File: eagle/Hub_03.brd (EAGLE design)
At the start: 24.3 x 59 mm, 16 parts, among them IC1 ATTINY85-20PU, Q1 IRFZ44NPBFS

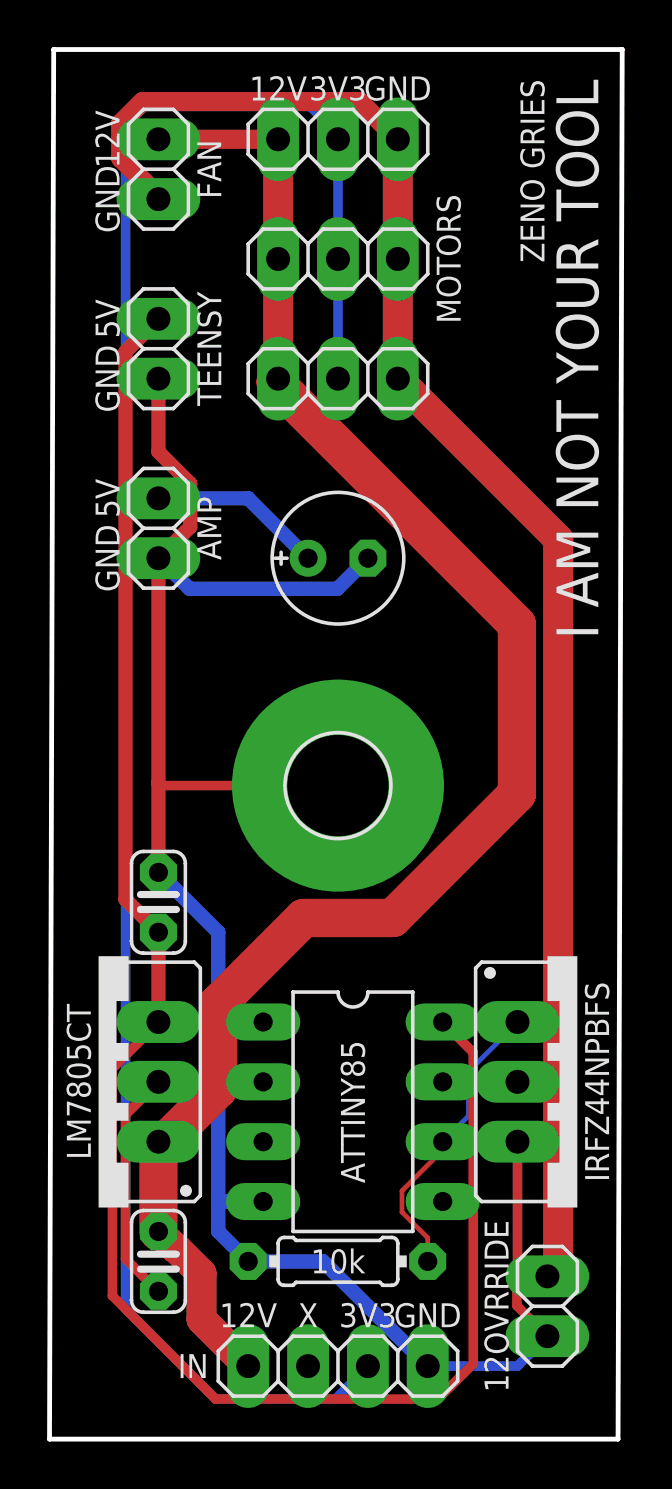
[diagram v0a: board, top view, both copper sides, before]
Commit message: added new hub
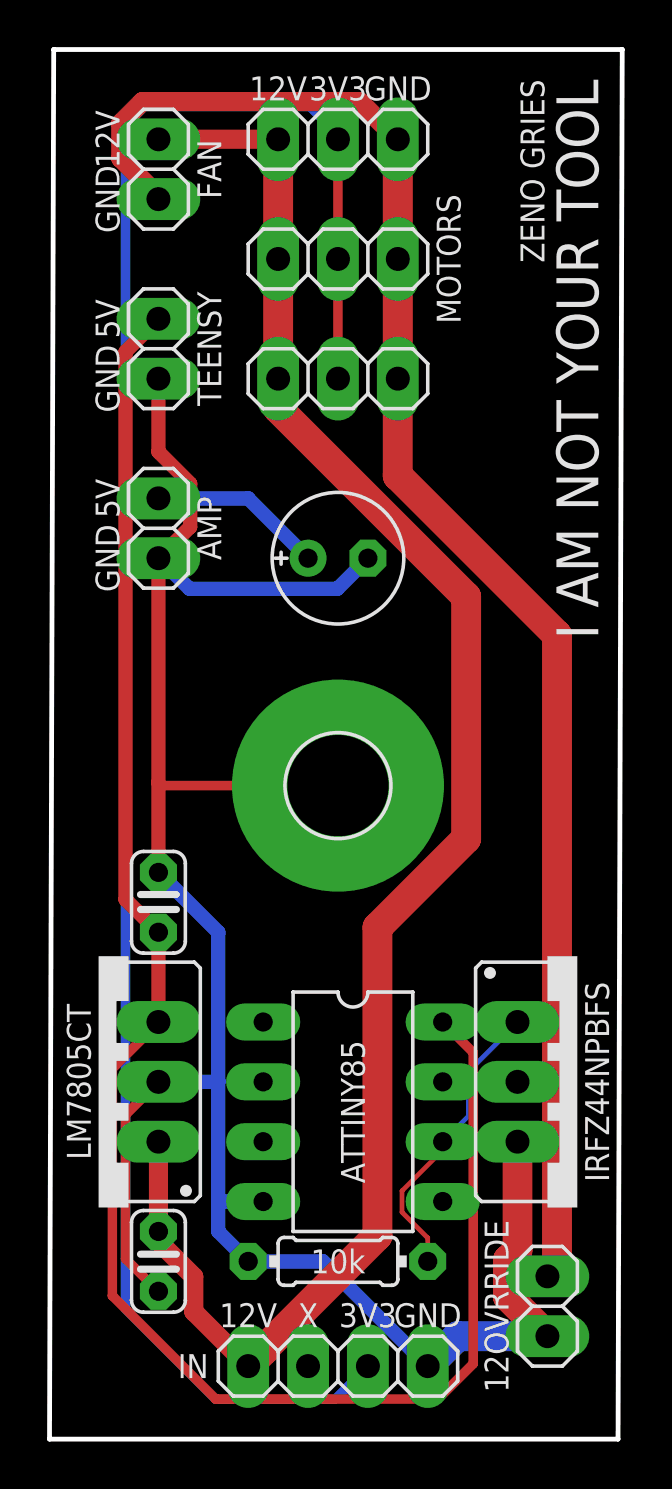
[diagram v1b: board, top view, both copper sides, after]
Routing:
- net MOTOR: track 122.7 -> 69.6 mm
- net +12V: track 89.6 -> 75.4 mm
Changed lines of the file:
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@@
 <wire x1="0" y1="29.21" x2="0.0198625" y2="29.21" width="0.6096" layer="1"/>
 <wire x1="1.3462" y1="32.3794625" x2="0" y2="33.7256625" width="0.6096" layer="1"/>
-<wire x1="11.43" y1="-5.08" x2="15.24" y2="-5.08" width="0.4064" layer="16"/>
-<wire x1="15.24" y1="-5.08" x2="16.51" y2="-3.81" width="0.4064" layer="16"/>
-<wire x1="15.2146" y1="-0.733425" x2="15.2146" y2="-2.517775" width="0.4064" layer="1"/>
-<wire x1="16.51" y1="-3.81" x2="16.506825" y2="-3.81" width="0.4064" layer="1"/>
-<wire x1="16.506825" y1="-3.81" x2="15.2146" y2="-2.517775" width="0.4064" layer="1"/>
-<wire x1="15.24" y1="4.445" x2="15.24" y2="-0.708025" width="0.4064" layer="1"/>
-<wire x1="15.24" y1="-0.708025" x2="15.2146" y2="-0.733425" width="0.4064" layer="1"/>
 <wire x1="7.62" y1="19.558" x2="0.127" y2="19.558" width="0.4064" layer="1"/>
 <wire x1="0.127" y1="19.558" x2="0" y2="19.685" width="0.4064" layer="1"/>
@@
 <wire x1="-0.01369375" y1="-1.905" x2="-1.397" y2="-0.52169375" width="0.4064" layer="1"/>
 <wire x1="-1.397" y1="-0.52169375" x2="-1.397" y2="5.5824625" width="0.4064" layer="1"/>
+<wire x1="11.43" y1="-5.08" x2="12.7" y2="-3.81" width="1.27" layer="16"/>
+<wire x1="12.7" y1="-3.81" x2="16.51" y2="-3.81" width="1.27" layer="16"/>
+<wire x1="14.8336" y1="-0.57560625" x2="15.24" y2="-0.16920625" width="1.27" layer="1"/>
+<wire x1="15.24" y1="-0.16920625" x2="15.24" y2="4.445" width="1.27" layer="1"/>
+<wire x1="16.51" y1="-3.81" x2="14.8336" y2="-2.1336" width="1.27" layer="1"/>
+<wire x1="14.8336" y1="-2.1336" x2="14.8336" y2="-0.57560625" width="1.27" layer="1"/>
 </signal>
 <signal name="+12V" class="2">
@@
 <contactref element="IN" pad="4"/>
 <contactref element="C5" pad="1"/>
-<wire x1="0" y1="4.445" x2="0.19" y2="4.445" width="1.27" layer="16"/>
-<wire x1="5.08" y1="36.83" x2="5.08" y2="41.91" width="1.27" layer="16"/>
-<wire x1="5.08" y1="41.91" x2="5.08" y2="46.99" width="1.27" layer="16"/>
-<wire x1="0" y1="4.445" x2="0.19" y2="4.445" width="1.27" layer="1"/>
+<wire x1="0" y1="46.99" x2="5.08" y2="46.99" width="0.8128" layer="1"/>
+<wire x1="3.81" y1="-5.08" x2="4.5212" y2="-4.3688" width="1.27" layer="1"/>
+<wire x1="4.5212" y1="-4.3688" x2="4.5212" y2="-4.32248125" width="1.27" layer="1"/>
+<wire x1="4.5212" y1="-4.32248125" x2="9.2964" y2="0.45271875" width="1.27" layer="1"/>
+<wire x1="9.2964" y1="0.45271875" x2="9.2964" y2="13.54135625" width="1.27" layer="1"/>
+<wire x1="9.2964" y1="13.54135625" x2="13.0598" y2="17.30475625" width="1.27" layer="1"/>
+<wire x1="13.0598" y1="27.5802" x2="5.08" y2="35.56" width="1.27" layer="1"/>
+<wire x1="5.08" y1="35.56" x2="5.08" y2="36.83" width="1.27" layer="1"/>
+<wire x1="13.0598" y1="17.30475625" x2="13.0598" y2="27.5802" width="1.27" layer="1"/>
 <wire x1="5.08" y1="36.83" x2="5.08" y2="41.91" width="1.27" layer="1"/>
 <wire x1="5.08" y1="41.91" x2="5.08" y2="46.99" width="1.27" layer="1"/>
-<wire x1="1.8288" y1="-1.14748125" x2="0.75751875" y2="-0.0762" width="1.27" layer="16"/>
-<wire x1="3.81" y1="-5.08" x2="1.8288" y2="-3.0988" width="1.27" layer="16"/>
-<wire x1="0.75751875" y1="-0.0762" x2="0.7112" y2="-0.0762" width="1.27" layer="16"/>
-<wire x1="0.7112" y1="-0.0762" x2="0" y2="0.635" width="1.27" layer="16"/>
-<wire x1="1.8288" y1="-3.0988" x2="1.8288" y2="-1.14748125" width="1.27" layer="16"/>
-<wire x1="1.8288" y1="-1.14748125" x2="0.75751875" y2="-0.0762" width="1.27" layer="1"/>
-<wire x1="3.81" y1="-5.08" x2="1.8288" y2="-3.0988" width="1.27" layer="1"/>
-<wire x1="0.75751875" y1="-0.0762" x2="0.7112" y2="-0.0762" width="1.27" layer="1"/>
-<wire x1="0.7112" y1="-0.0762" x2="0" y2="0.635" width="1.27" layer="1"/>
-<wire x1="1.8288" y1="-3.0988" x2="1.8288" y2="-1.14748125" width="1.27" layer="1"/>
-<wire x1="0" y1="46.99" x2="5.08" y2="46.99" width="0.8128" layer="1"/>
-<wire x1="0" y1="0.635" x2="0" y2="4.445" width="1.6256" layer="1"/>
-<wire x1="0" y1="4.445" x2="0.2977625" y2="4.445" width="1.6256" layer="1"/>
-<wire x1="2.54" y1="6.6872375" x2="0.2977625" y2="4.445" width="1.6256" layer="1"/>
-<wire x1="2.54" y1="6.6872375" x2="2.54" y2="10.31408125" width="1.6256" layer="1"/>
-<wire x1="2.54" y1="10.31408125" x2="6.16631875" y2="13.9404" width="1.6256" layer="1"/>
-<wire x1="6.16631875" y1="13.9404" x2="9.9468875" y2="13.9404" width="1.6256" layer="1"/>
-<wire x1="9.9468875" y1="13.9404" x2="15.2146" y2="19.2081125" width="1.6256" layer="1"/>
-<wire x1="5.08" y1="36.83" x2="4.9784" y2="36.7284" width="1.6256" layer="1"/>
-<wire x1="4.9784" y1="36.7284" x2="4.9784" y2="36.6338375" width="1.6256" layer="1"/>
-<wire x1="15.2146" y1="26.3976375" x2="4.9784" y2="36.6338375" width="1.6256" layer="1"/>
-<wire x1="15.2146" y1="19.2081125" x2="15.2146" y2="26.3976375" width="1.6256" layer="1"/>
+<wire x1="3.81" y1="-5.08" x2="1.4986" y2="-2.7686" width="0.8128" layer="1"/>
+<wire x1="0" y1="0.21434375" x2="0" y2="0.635" width="0.8128" layer="1"/>
+<wire x1="1.4986" y1="-2.7686" x2="1.4986" y2="-1.28425625" width="0.8128" layer="1"/>
+<wire x1="1.4986" y1="-1.28425625" x2="0" y2="0.21434375" width="0.8128" layer="1"/>
+<wire x1="0" y1="0.635" x2="0" y2="4.445" width="0.8128" layer="1"/>
 </signal>
 <signal name="+5V" class="3">
@@
 <wire x1="7.62" y1="46.99" x2="7.62" y2="47.20434375" width="0.4064" layer="16"/>
 <wire x1="7.62" y1="47.20434375" x2="6.43734375" y2="48.387" width="0.4064" layer="16"/>
-<wire x1="7.62" y1="46.99" x2="7.62" y2="41.91" width="0.4064" layer="16"/>
-<wire x1="7.62" y1="41.91" x2="7.62" y2="36.83" width="0.4064" layer="16"/>
 <wire x1="8.89" y1="-5.1054" x2="8.89" y2="-5.08" width="0.4064" layer="16"/>
 <wire x1="8.89" y1="-5.1054" x2="7.5184" y2="-6.477" width="0.4064" layer="16"/>
 <wire x1="2.42650625" y1="-6.477" x2="7.5184" y2="-6.477" width="0.4064" layer="16"/>
+<wire x1="7.62" y1="46.99" x2="7.62" y2="41.91" width="0.4064" layer="1"/>
+<wire x1="7.62" y1="41.91" x2="7.62" y2="36.83" width="0.4064" layer="1"/>
 </signal>
 <signal name="MOTOR" class="1">
@@
 <contactref element="FAN" pad="1"/>
 <contactref element="MOTORSWITCH" pad="2"/>
-<wire x1="16.9672" y1="30.0228" x2="16.9672" y2="6.985" width="1.27" layer="16"/>
-<wire x1="16.9672" y1="6.985" x2="16.9672" y2="-0.8128" width="1.27" layer="16"/>
-<wire x1="16.51" y1="-1.27" x2="16.9672" y2="-0.8128" width="1.27" layer="16"/>
-<wire x1="16.9672" y1="30.0228" x2="10.16" y2="36.83" width="1.27" layer="16"/>
-<wire x1="10.16" y1="36.83" x2="10.16" y2="41.91" width="1.27" layer="16"/>
-<wire x1="10.16" y1="41.91" x2="10.16" y2="46.99" width="1.27" layer="16"/>
-<wire x1="16.9672" y1="30.0228" x2="16.9672" y2="6.985" width="1.27" layer="1"/>
-<wire x1="16.9672" y1="6.985" x2="16.9672" y2="-0.8128" width="1.27" layer="1"/>
-<wire x1="16.51" y1="-1.27" x2="16.9672" y2="-0.8128" width="1.27" layer="1"/>
-<wire x1="16.9672" y1="30.0228" x2="10.16" y2="36.83" width="1.27" layer="1"/>
-<wire x1="10.16" y1="36.83" x2="10.16" y2="41.91" width="1.27" layer="1"/>
-<wire x1="10.16" y1="41.91" x2="10.16" y2="46.99" width="1.27" layer="1"/>
-<wire x1="15.24" y1="6.985" x2="16.9672" y2="6.985" width="1.27" layer="16"/>
-<wire x1="15.24" y1="6.985" x2="16.9672" y2="6.985" width="1.27" layer="1"/>
 <wire x1="-1.6002" y1="46.1834875" x2="-1.6002" y2="47.6695125" width="0.8128" layer="1"/>
 <wire x1="-1.6002" y1="47.6695125" x2="-0.6795125" y2="48.5902" width="0.8128" layer="1"/>
@@
 <wire x1="0" y1="44.45" x2="0" y2="44.5832875" width="0.8128" layer="1"/>
 <wire x1="0" y1="44.5832875" x2="-1.6002" y2="46.1834875" width="0.8128" layer="1"/>
+<wire x1="16.9164" y1="25.95070625" x2="16.9164" y2="6.985" width="1.27" layer="1"/>
+<wire x1="16.9164" y1="6.985" x2="16.9164" y2="-0.8636" width="1.27" layer="1"/>
+<wire x1="16.51" y1="-1.27" x2="16.9164" y2="-0.8636" width="1.27" layer="1"/>
+<wire x1="16.9164" y1="25.95070625" x2="10.155953125" y2="32.711153125" width="1.27" layer="1"/>
+<wire x1="10.155953125" y1="32.711153125" x2="10.155953125" y2="36.825953125" width="1.27" layer="1"/>
+<wire x1="10.155953125" y1="36.825953125" x2="10.16" y2="36.83" width="1.27" layer="1"/>
+<wire x1="10.16" y1="36.83" x2="10.16" y2="41.91" width="1.27" layer="1"/>
+<wire x1="10.16" y1="41.91" x2="10.16" y2="46.97574375" width="1.27" layer="1"/>
+<wire x1="10.16" y1="46.97574375" x2="10.14574375" y2="46.99" width="1.27" layer="1"/>
+<wire x1="15.24" y1="6.985" x2="16.9164" y2="6.985" width="1.27" layer="1"/>
 </signal>
 <signal name="N$1">
